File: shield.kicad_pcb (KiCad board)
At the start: 4 copper layers, 150 x 120 mm, 158 parts, among them J1 NAPPE_ADC1, J10 OLED_SPI_2x8, J13 NAPPE_LOGIC, J14 NAPPE_COM, J2 NAPPE_ADC2, J3 NAPPE_PWM, J4 NAPPE_GPIO1, J5 DEVKIT_C2000_ROW_A, J6 DEVKIT_C2000_ROW_B, J7 ESP32_C6_DEVKITC_1_J1, J8 ESP32_C6_DEVKITC_1_J3, J9 J_PWR_11-25V, U1 LDO_3V3_ISO, U2 NCM3S1205MC, U3 NCM3S1205MC, U4 ER-OLEDM032-1

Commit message: Corrige 45 footprints B.Cu dont la serigraphie/fab/courtyard restait sur la face avant
Signale par l'utilisateur en vue 3D (groupe D4/R3/C3 correct vs groupe
D9/R7/C7 absent). Verifie sur les 158 footprints : 45 montes en B.Cu
(D25-D39/R24-R38/C44-C58, issus des generations en masse des decisions
#19/#20) gardaient des elements F.SilkS/F.CrtYd/F.Fab au lieu de leurs
equivalents B.*. Corrige par negation du Y local + permutation de
couche, verifie element par element contre un trio correct (D36/R3/C3)
avant generalisation. Script de verification reutilisable ajoute
(check_mirrored_footprints.py, racine du workspace), et la methode
KICAD-EDITION-GROUPEE-KIPY.md mise a jour (iterer sur tous les champs
d'un footprint, pas une liste fermee ; verifier kipy.KiCad() avant
d'editer un .kicad_pcb en texte si KiCad peut l'avoir ouvert).

DRC (hors unconnected_items, stable a 313) : 412 -> 382.
lib_footprint_mismatch 36->0, npth_inside_courtyard 2->0,
courtyards_overlap 2->1, silk_over_copper 80->75. silk_overlap 41->55
(14 chevauchements reels entre trios voisins, desormais detectables
puisque les deux cotes sont enfin sur la meme couche - point ouvert de
layout, non traite ici). clearance et text_height inchanges.

Co-Authored-By: Claude Sonnet 5 <noreply@anthropic.com>
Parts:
- removed C36, C37: 100uF, Capacitor_SMD:C_1210_3225Metric
- added C59: 100uF 50V, Capacitor_SMD:CP_Elec_8x10.5, F.Cu at (123.8, 129.2)
- added C60: 100uF 50V, Capacitor_SMD:CP_Elec_8x10.5, F.Cu at (133.5, 66.2)
- moved C41 30.8 mm to (164.8, 59.3)
- moved C40 30.8 mm to (164.8, 45.9)
- moved D1 30.8 mm to (121.7, 52.7)
- moved J9 30.8 mm to (131.8, 39.1)
- moved U1 30.8 mm to (128.9, 52.8)
- moved U3 30.8 mm to (147.9, 52.8)
- moved U2 25.6 mm to (186.3, 52.8)
- moved U4 21.6 mm to (160.3, 51.6)
- moved JP3 7.61 mm to (119.2, 74.0)
- moved JP2 7.47 mm to (159.8, 76.0)
- moved J6 3.76 mm to (175.3, 81.7)
- moved J5 3.76 mm to (152.4, 81.7)
- moved J7 3.71 mm to (115.0, 81.7)
- moved J8 3.71 mm to (137.9, 81.7)

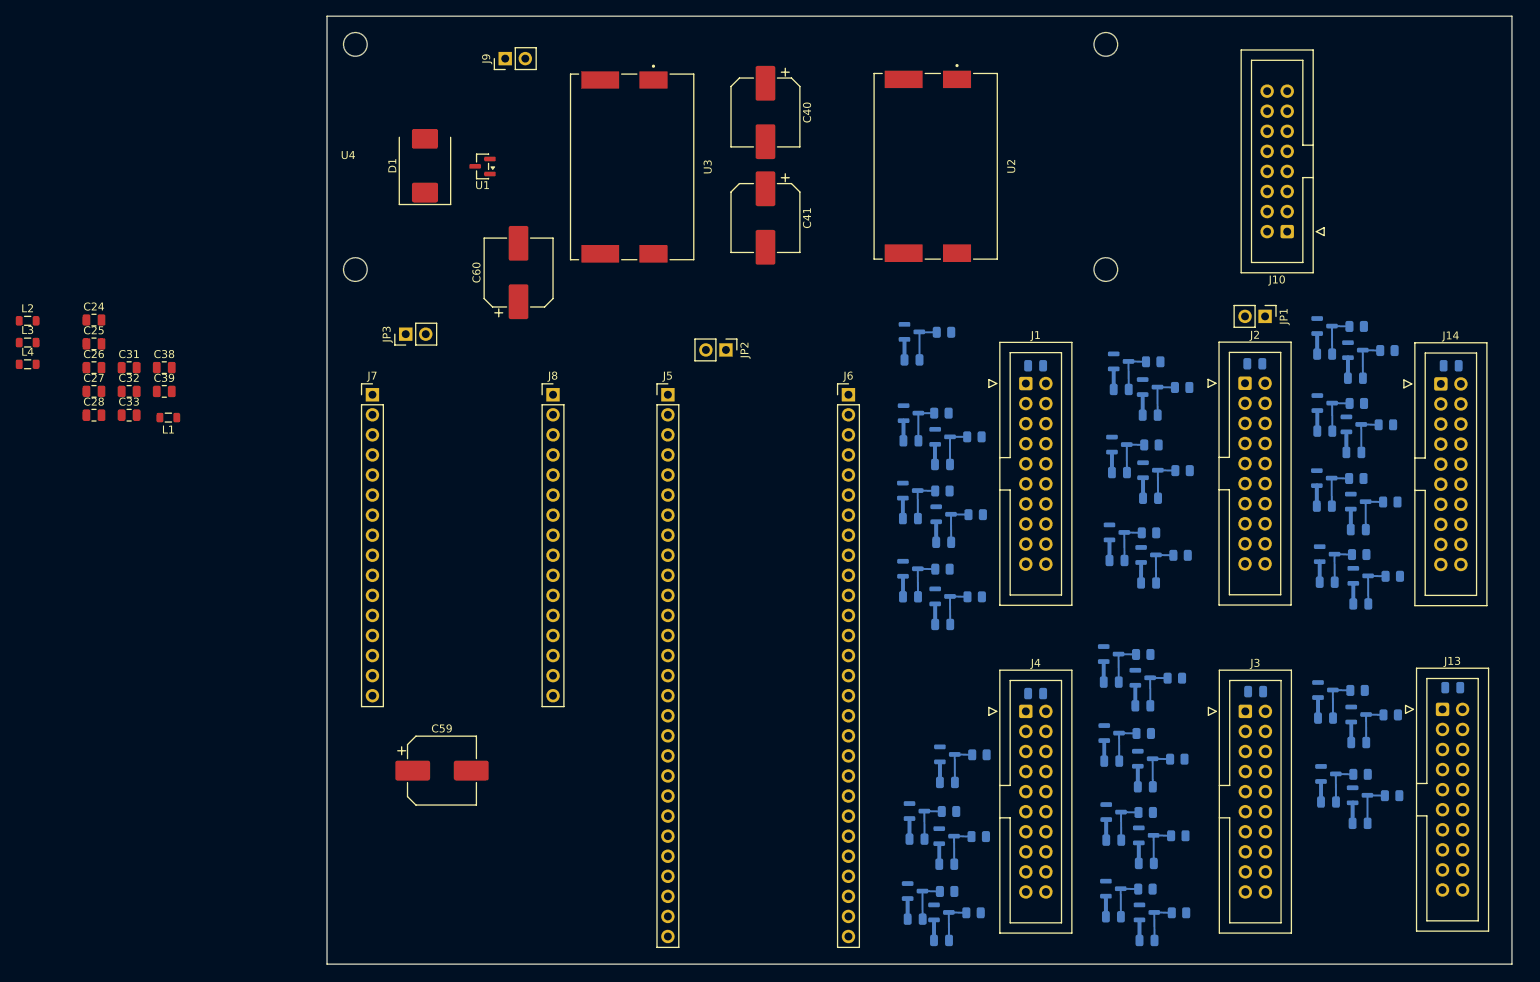
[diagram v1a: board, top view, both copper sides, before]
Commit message: Ajoute le filtre EMC FL3/FL4 (U3), corrige les caps de sortie 100uF et le rendu 3D du devkit/NCM3S1205MC
- dc.kicad_sch : ajoute FL3/FL4 (Bourns SRF0905) sur le filtre EMC de
  U3, empreinte lib:Filter_Bourns_SRF0905_6.0x9.2mm_My
- connecteur_devkit.kicad_sch : C36/C37 renommes C59/C60, passent en
  100uF 50V / CP_Elec_8x10.5 (electrolytique) au lieu du MLCC 1210 ;
  embases devkit en PinSocket (femelle) au lieu de PinHeader
- connecteurs_nappe/protection_nappe.kicad_sch : complete les labels
  nappe manquants (Discharge, PWM3_B, PWM4_B, Stage2_EN)
- lib/ER-OLEDM032-1.kicad_mod, lib/NCM3S1205MC.kicad_mod : corrige
  l'orientation/offset des modeles 3D (STEP mal aligne)
- lib/DLW5BSZ801TQ2L.step : nouveau modele 3D
- shield.kicad_pcb/.kicad_pro : presets de piste/via supplementaires,
  remove_islands actif
- README.md + doc/shield.png : ajoute le rendu 3D de la carte

Verification avant commit : kicad-cli sch erc (233 violations, 35
erreurs) et pcb drc (329 violations + 183 non connectes) --
inchange dans sa nature par rapport aux sessions precedentes, rien
corrige ici qui ne decoule pas des changements ci-dessus (regle
KICAD.md : rapporter, pas corriger d'office).

Co-Authored-By: Claude Sonnet 5 <noreply@anthropic.com>
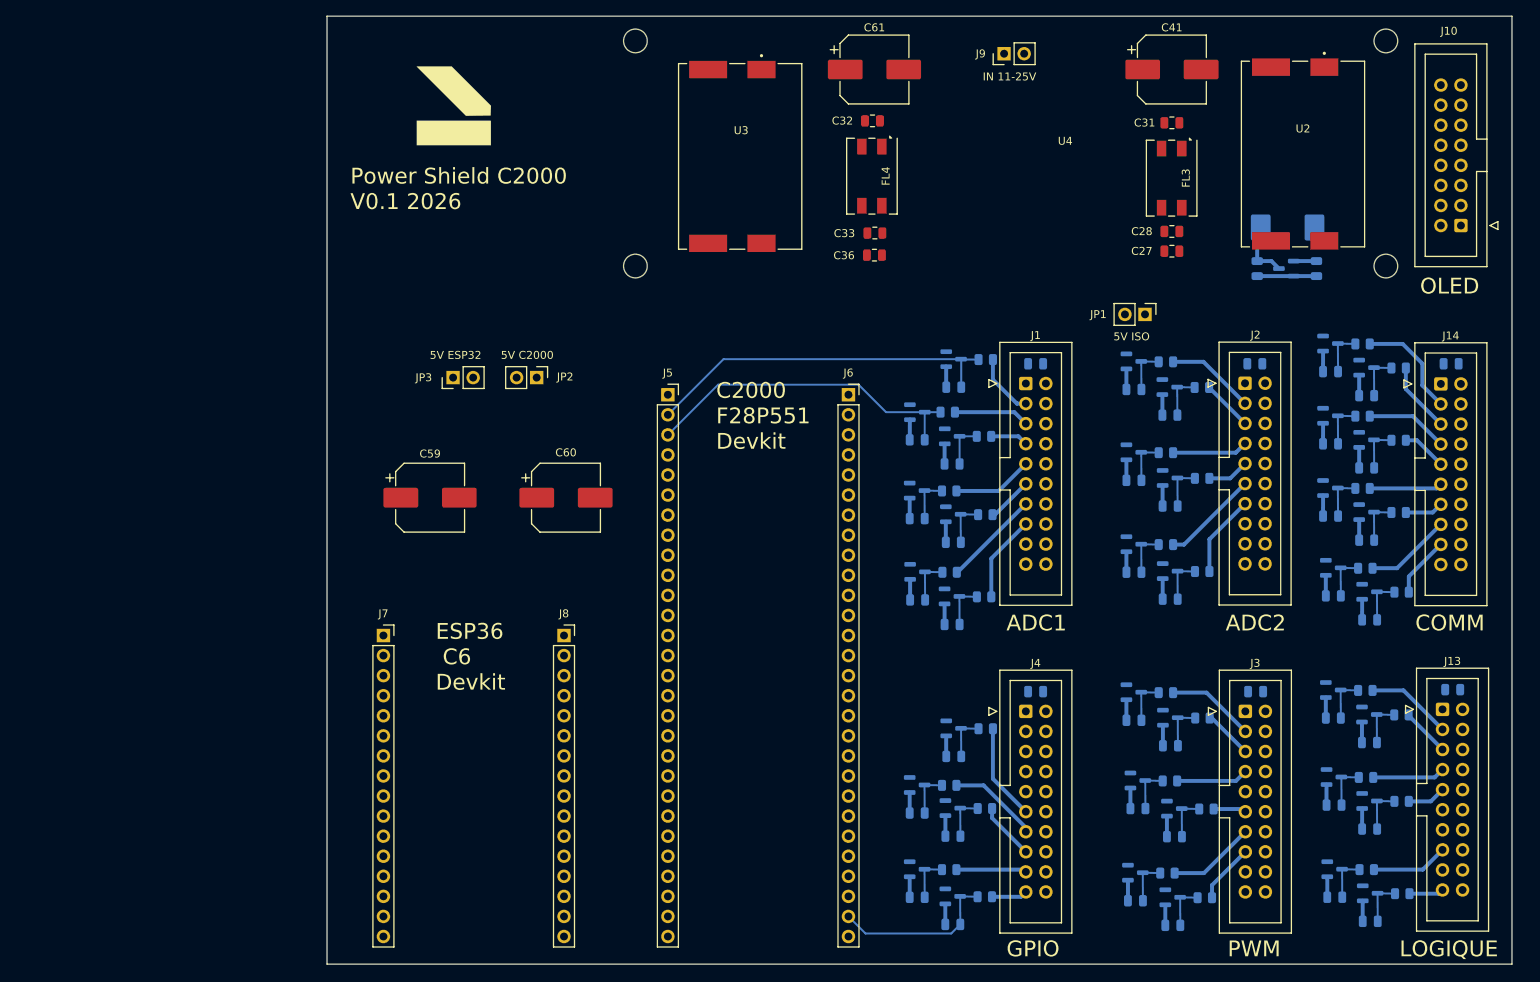
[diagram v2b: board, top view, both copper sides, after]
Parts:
- removed C24, C25: 100nF, Capacitor_SMD:C_0805_2012Metric
- removed C26: 22uF, Capacitor_SMD:C_0805_2012Metric
- removed C40: 100uF 50V, Capacitor_SMD:CP_Elec_8x10.5
- removed L1, L2, L3, L4: 22uH, Inductor_SMD:L_0805_2012Metric
- added C36: 10uF, Capacitor_SMD:C_0805_2012Metric, F.Cu at (178.6, 64.0)
- added C61: 100uF 50V, Capacitor_SMD:CP_Elec_8x10.5, F.Cu at (178.6, 40.5)
- added FL3: Choke_CommonMode_FerriteCore_1423, lib:Filter_Bourns_SRF0905_6.0x9.2mm_My, F.Cu at (216.2, 54.2)
- added FL4: Choke_CommonMode_FerriteCore_1423, lib:Filter_Bourns_SRF0905_6.0x9.2mm_My, F.Cu at (178.2, 54.0)
- added Lebel Audio: LOGO, lib:lebel-logo, F.Cu at (125.6, 45.1)
- C27: value 22uF -> 10uF
- C28, C33: value 220pF -> 1nF
- C31, C32: value 22uF -> 100nF
- C38, C39, D1, U1: moved to B.Cu
- J5, J6: footprint Connector_PinHeader_2.54mm:PinHeader_1x28_P2.54mm_Vertical -> Connector_PinSocket_2.54mm:PinSocket_1x28_P2.54mm_Vertical
- J7, J8: footprint Connector_PinHeader_2.54mm:PinHeader_1x16_P2.54mm_Vertical -> Connector_PinSocket_2.54mm:PinSocket_1x16_P2.54mm_Vertical
- moved C38 146.4 mm to (234.5, 65.7), turned to -90 degrees
- moved C39 139.2 mm to (227.0, 65.7), turned to -90 degrees
- moved C28 138.4 mm to (216.2, 61.0)
- moved C27 137.6 mm to (216.2, 63.5)
- moved C31 135.6 mm to (216.2, 47.2)
- moved D1 109.5 mm to (230.8, 60.5), turned to 0 degrees
- moved U1 102.6 mm to (230.7, 65.7)
- moved C32 100.1 mm to (178.3, 47.0)
- moved C33 97.2 mm to (178.6, 61.2)
- moved J9 63.2 mm to (195.0, 38.5)
- moved C41 54.8 mm to (216.2, 40.5), turned to 0 degrees
- moved U2 46.5 mm to (232.8, 51.2)
- moved U4 35.5 mm to (195.8, 51.1)
- moved C59 34.6 mm to (122.3, 94.7)
- moved J7 30.5 mm to (116.4, 112.2)
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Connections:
- C27 pad 1: U2_VINF -> U2_GNDF
- C27 pad 2: U2_GNDF -> U2_VINF
- C31 pad 1: U3_VINF -> VIN_PWR
- C31 pad 2: U3_GNDF -> GND_PRI
- C32 pad 1: U3_VINF -> VIN_PWR
- C32 pad 2: U3_GNDF -> GND_PRI
- C41 pad 1: U3_VINF -> VIN_PWR
- C41 pad 2: U3_GNDF -> GND_PRI
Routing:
- net Vin_MCU: track 5.76 -> 45.8 mm
- net Vout_MCU: track 5.50 -> 42.1 mm
- net CLB_OUT_MCU: track 5.76 -> 21.3 mm
- net UART_TX: track 0.00 -> 13.8 mm
- net Iin: track 0.00 -> 12.3 mm
- net I_SHUNT1_CMP: track 0.00 -> 12.3 mm
- net CMP_OUT: track 0.00 -> 12.2 mm
- net nFAULT: track 0.00 -> 11.5 mm
- net VREFLO_SENSE: track 0.00 -> 11.3 mm
- net PWM1_A: track 0.00 -> 11.2 mm
- net PWM3_B: track 0.00 -> 11.1 mm
- net Iout: track 0.00 -> 11.0 mm
- net CAN_TX: track 0.00 -> 10.9 mm
- net Stage1_EN: track 0.00 -> 10.9 mm
- net SPI_CLK: track 0.00 -> 10.5 mm
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- added copper zone on In1.Cu, net GND
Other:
- board text added: "5V C2000"
- board text added: "5V ESP32"
- board text added: "5V ISO"
- board text added: "ADC1"
- board text added: "ADC2"
- board text added: "C2000 F28P551 Devkit"
- board text added: "COMM"
- board text added: "ESP36 C6 Devkit"
- board text added: "GPIO"
- board text added: "IN 11-25V"
- board text added: "LOGIQUE"
- board text added: "OLED"
- board text added: "PWM"
- board text added: "Power Shield C2000 V0.1 2026"
